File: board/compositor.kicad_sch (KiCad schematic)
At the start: 2 parts, among them U21 COMPOSITOR

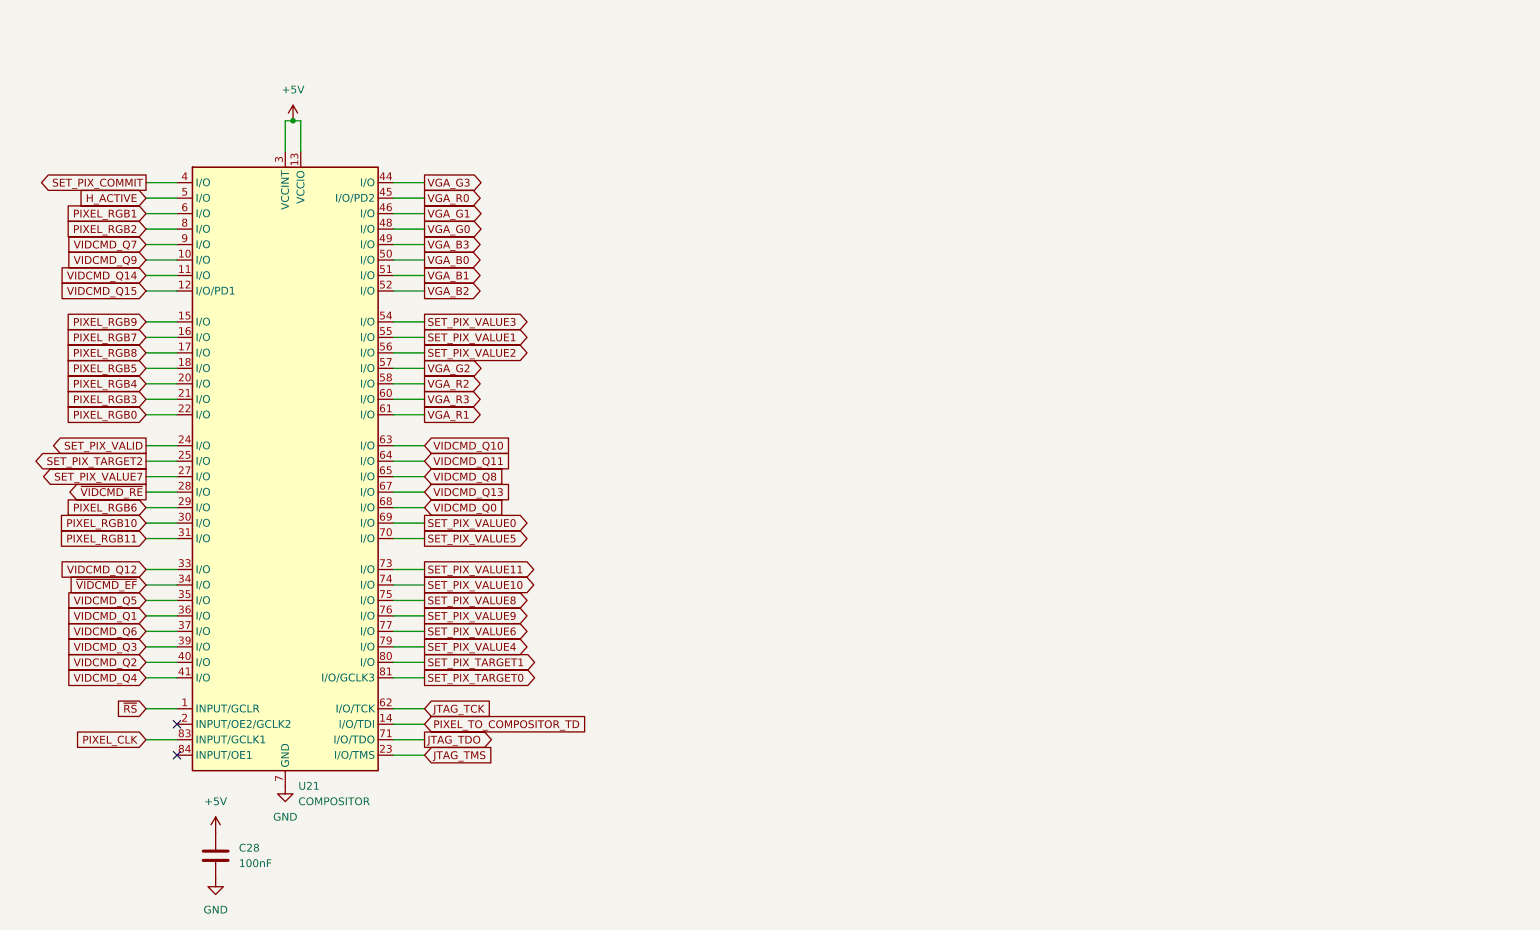
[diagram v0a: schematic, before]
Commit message: add VIDCMD FIFOs; FIFO strobe termination becomes a 0R-stuffed footprint
Co-Authored-By: Claude Fable 5.1 <noreply@anthropic.com>
Claude-Session: https://claude.ai/code/session_01NsFH8WNb3Tja14xUfwuyqj
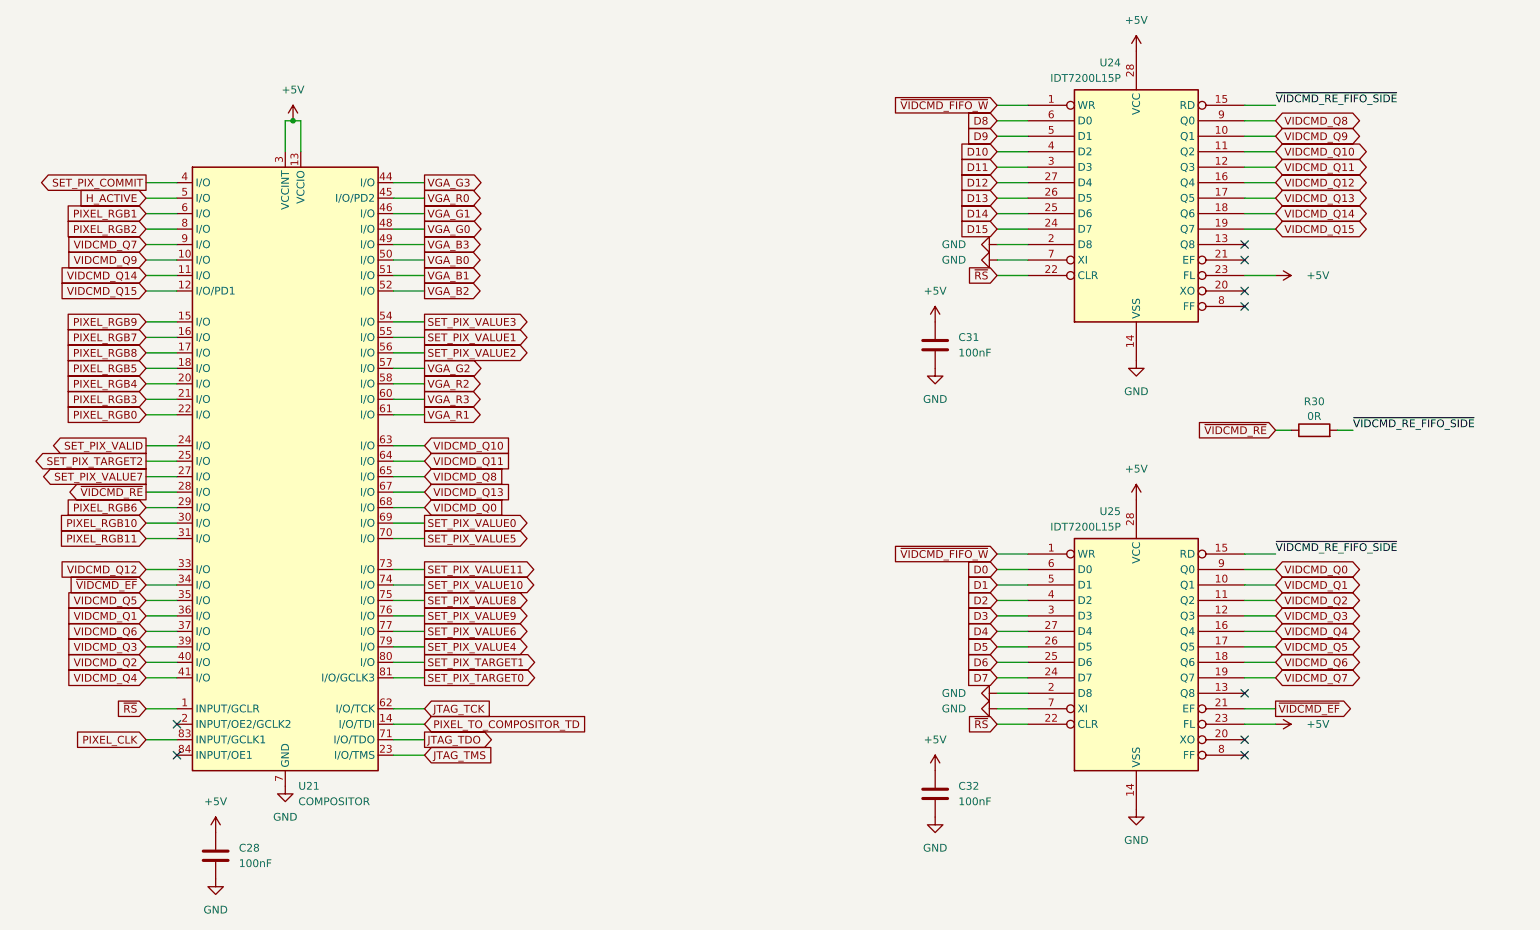
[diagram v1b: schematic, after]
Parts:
- added C31, C32: 100nF, Capacitor_THT:C_Disc_D5.0mm_W2.5mm_P5.00mm, symbol Device:C
- added R30: 0R, Resistor_THT:R_Axial_DIN0207_L6.3mm_D2.5mm_P10.16mm_Horizontal, symbol Device:R
- added U24, U25: IDT7200L15P, Package_DIP:DIP-28_W7.62mm, symbol Memory_RAM:IDT7201
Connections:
- net +5V: now also C31.1, C32.1, U24.23 (FL), U24.28 (VCC), U25.23 (FL), U25.28 (VCC)
- net GND: now also C31.2, C32.2, U24.14 (VSS), U24.2 (D8), U24.7 (XI), U25.14 (VSS), U25.2 (D8), U25.7 (XI)
- net VIDCMD_Q0: now also U25.9 (Q0)
- net VIDCMD_Q1: now also U25.10 (Q1)
- net VIDCMD_Q10: now also U24.11 (Q2)
- net VIDCMD_Q11: now also U24.12 (Q3)
- net VIDCMD_Q12: now also U24.16 (Q4)
- net VIDCMD_Q13: now also U24.17 (Q5)
- net VIDCMD_Q14: now also U24.18 (Q6)
- net VIDCMD_Q15: now also U24.19 (Q7)
- net VIDCMD_Q2: now also U25.11 (Q2)
- net VIDCMD_Q3: now also U25.12 (Q3)
- net VIDCMD_Q4: now also U25.16 (Q4)
- net VIDCMD_Q5: now also U25.17 (Q5)
- net VIDCMD_Q6: now also U25.18 (Q6)
- net VIDCMD_Q7: now also U25.19 (Q7)
- net VIDCMD_Q8: now also U24.9 (Q0)
- net VIDCMD_Q9: now also U24.10 (Q1)
- net ~{RS}: now also U24.22 (CLR), U25.22 (CLR)
- net ~{VIDCMD_EF}: now also U25.21 (EF)
- net ~{VIDCMD_RE}: now also R30.1
- new net D0: U25.6 (D0)
- new net D1: U25.5 (D1)
- new net D10: U24.4 (D2)
- new net D11: U24.3 (D3)
- new net D12: U24.27 (D4)
- new net D13: U24.26 (D5)
- new net D14: U24.25 (D6)
- new net D15: U24.24 (D7)
- new net D2: U25.4 (D2)
- new net D3: U25.3 (D3)
- new net D4: U25.27 (D4)
- new net D5: U25.26 (D5)
- new net D6: U25.25 (D6)
- new net D7: U25.24 (D7)
- new net D8: U24.6 (D0)
- new net D9: U24.5 (D1)
- new net ~{VIDCMD_FIFO_W}: U24.1 (WR), U25.1 (WR)
- new net ~{VIDCMD_RE_FIFO_SIDE}: R30.2, U24.15 (RD), U25.15 (RD)
- no-connect marks 2 -> 9
